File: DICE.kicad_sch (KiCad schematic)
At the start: 95 parts, among them J101 Conn_01x03_Pin, J102 AudioJack2, J103 AudioJack2, J104 AudioJack2, J105 AudioJack2, J106 AudioJack2, J107 AudioJack2, J108 Conn_02x05_Odd_Even, J109 Conn_01x03_Pin, J11 AudioJack2, J110 Conn_01x05_Pin, J111 Conn_01x05_Pin, J112 Conn_01x07_Pin, J113 Conn_01x07_Pin, J114 Conn_01x07_Pin, J115 Conn_01x07_Pin, J116 Conn_01x03_Pin, J117 Conn_01x03_Pin, J2 Conn_01x03_Pin, Q101 BC847, Q102 BC847, SW1 SW_SPDT, SW101 SW_SPDT, SW102 SW_SPDT, U1 TL074, U101 DG412xUE, U102 TL074, U103 TL074

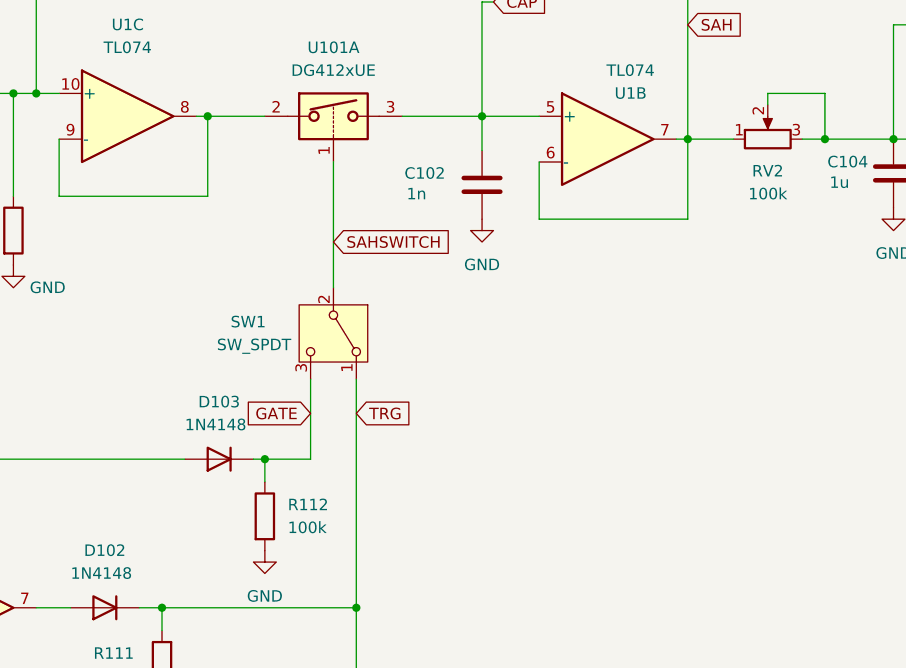
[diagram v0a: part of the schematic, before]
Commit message: Added TRG LED
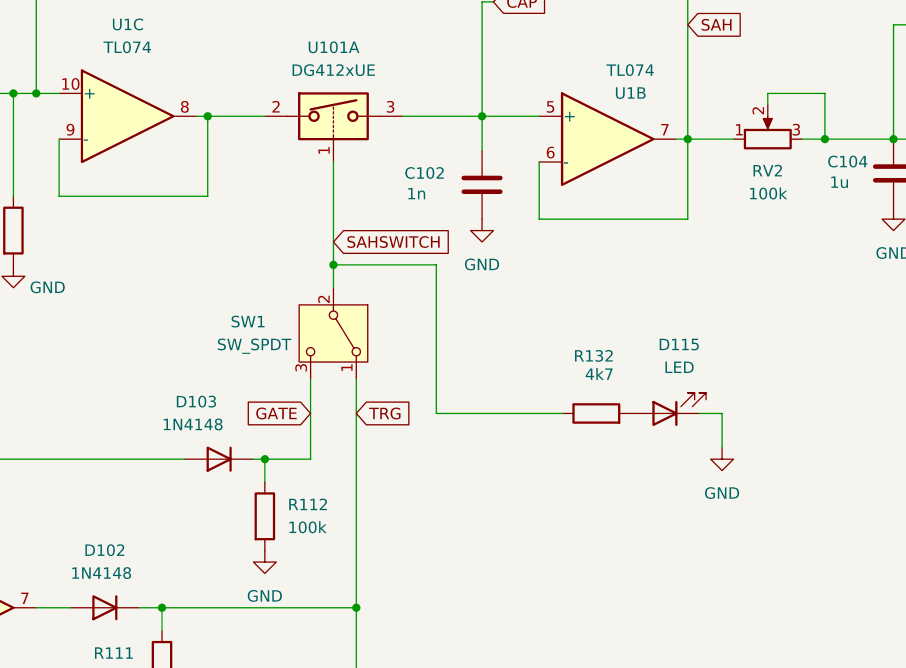
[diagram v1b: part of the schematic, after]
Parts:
- added D115: LED, LED_THT:LED_D3.0mm, symbol Device:LED
- added R132: 4k7, Resistor_SMD:R_1206_3216Metric, symbol Device:R
- C3: footprint 1u -> Capacitor_SMD:C_1206_3216Metric
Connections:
- net GND: now also D115.1 (K)
- net SAHSWITCH: now also R132.1
- new net: D115.2 (A), R132.2

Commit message: Added an LED indicator to the COMP output
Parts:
- added D116: LED, LED_THT:LED_D3.0mm, symbol Device:LED
- added Q103: BC847, Package_TO_SOT_SMD:SOT-23, symbol Transistor_BJT:BC847
- added R133: 4k7, Resistor_SMD:R_1206_3216Metric, symbol Device:R
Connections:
- net +12V: now also Q103.3 (C)
- net COMP: now also Q103.1 (B)
- net GND: now also D116.1 (K)
- new net: D116.2 (A), R133.2
- new net: Q103.2 (E), R133.1

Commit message: Fixed false positive triggers on COMP output
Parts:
- added D117: 1N4148, Diode_SMD:D_SOD-323_HandSoldering, symbol Device:D
- added R134: 1M, Resistor_SMD:R_1206_3216Metric, symbol Device:R
- R119: value 100k -> 47k
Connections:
- net COMP: now also Q103.2 (E), R120.1, R133.1; no longer J107.T, Q103.1 (B), R120.2
- net GND: now also R134.1; no longer R119.1
- net at R101.2, R102.2, U1.12 (+): no longer C101.2
- net at J109.1 (Pin_1), R119.2, U101.6: now also C101.2; no longer D104.1 (K), J2.2 (Pin_2)
- net at J109.2 (Pin_2): now also D104.2 (A); no longer R120.1
- net at U1.14: now also R119.1; no longer D104.2 (A)
- new net: J107.T, R120.2
- new net: D117.2 (A), J2.2 (Pin_2)
- new net: D104.1 (K), D117.1 (K), Q103.1 (B), R134.2
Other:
- note added: "Board Connectors"
- note added: "LED Indicators"
- moved on the sheet: C1, C101, C102, C103, C104, C105, C106, C107, C108, C2, C3, D10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
